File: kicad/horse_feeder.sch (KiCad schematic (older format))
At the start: 50 parts

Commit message: Update schematic
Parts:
- removed RV?: R_POT, symbol Device:R_POT
- removed U?: DS3231MZ, Package_SO:SOIC-8_3.9x4.9mm_P1.27mm, symbol Timer_RTC:DS3231MZ
- removed U?: NHD-0420H1Z, Display:NHD-0420H1Z, symbol Display_Character:NHD-0420H1Z
- added C?: C, symbol Device:C
- added D?: D, symbol Device:D
- added R? (x2): R, symbol Device:R
- added U?: NHD-C0220BIZ, Display:NHD-C0220BiZ, symbol Display_Character:NHD-C0220BIZ
- U? (x3): symbol custom_parts:TC4426ACPA -> horse_feeder-rescue:TC4426ACPA-custom_parts
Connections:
- net labels added: 3.3V, DPD_PIN
- net labels removed: LCD4, LCD5, LCD6, LCD7, LCD_BUS, LCD_EN, LCD_RS, LCD_RW, LOCKBUS
- wire segments 186 -> 166
- no-connect marks 22 -> 20
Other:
- moved on the sheet: R?, SW?

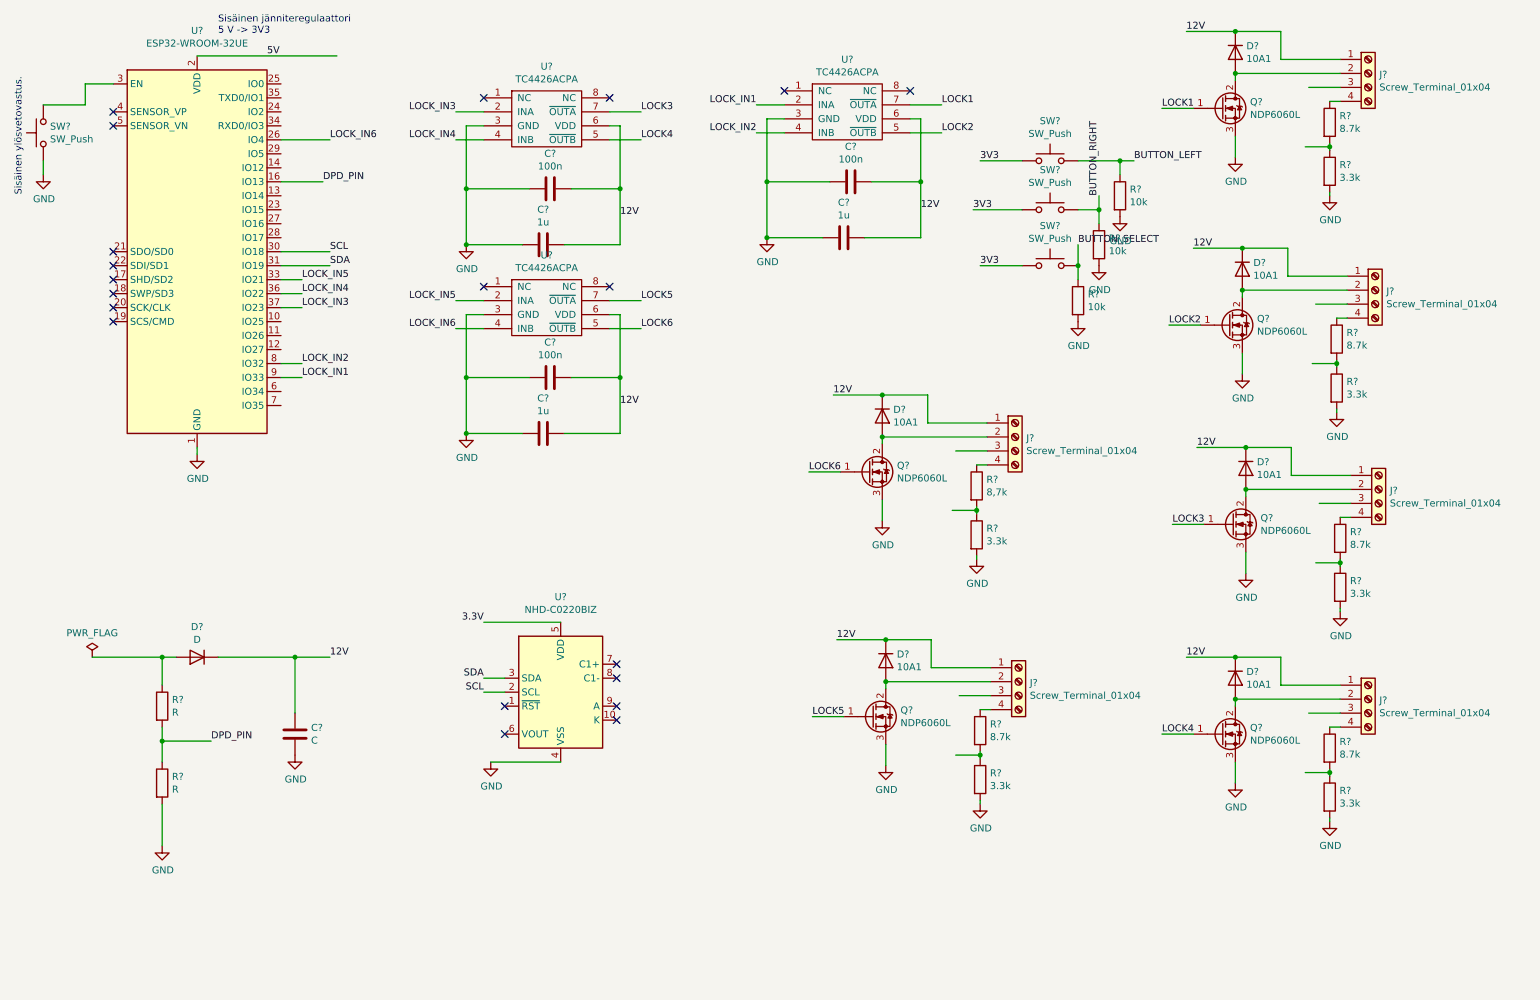
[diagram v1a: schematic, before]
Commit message: Modified schematic and PCB
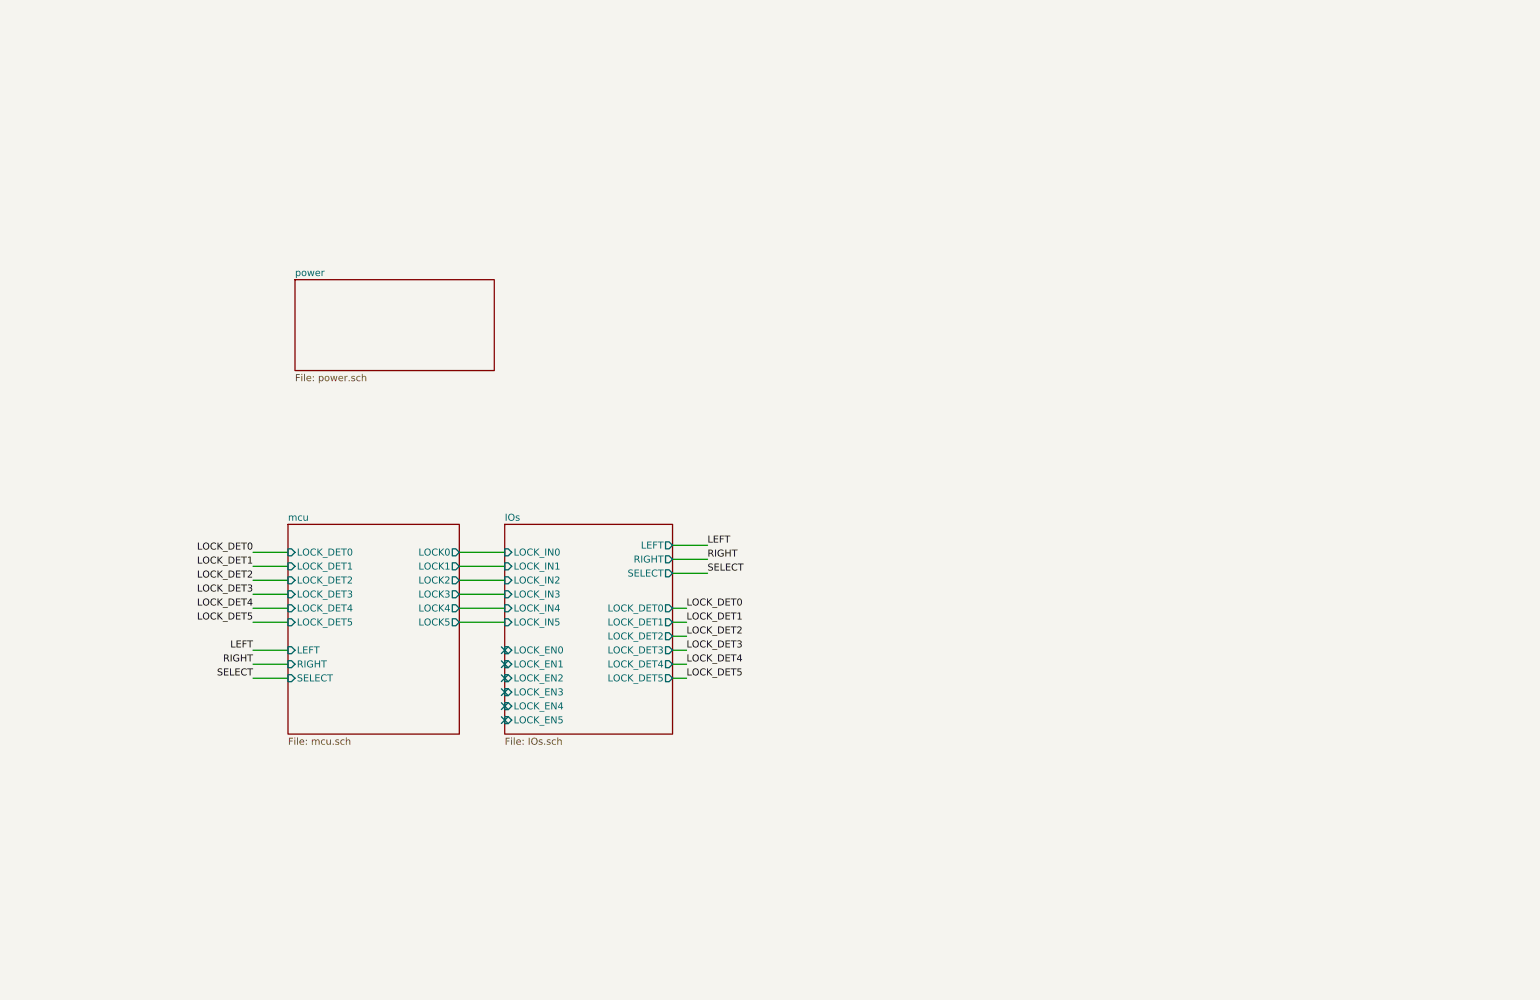
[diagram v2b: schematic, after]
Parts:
- removed C? (x3): 100n, symbol Device:C
- removed C? (x3): 1u, symbol Device:C
- removed C?: C, symbol Device:C
- removed D? (x6): 10A1, symbol Device:D
- removed D?: D, symbol Device:D
- removed J? (x6): Screw_Terminal_01x04, symbol Connector:Screw_Terminal_01x04
- removed Q? (x6): NDP6060L, symbol Device:Q_NMOS_GDS
- removed R? (x5): 8.7k, symbol Device:R
- removed R? (x6): 3.3k, symbol Device:R
- removed R?: 8,7k, symbol Device:R
- removed R? (x2): R, symbol Device:R
- removed R? (x3): 10k, symbol Device:R
- removed SW? (x4): SW_Push, symbol Switch:SW_Push
- removed U? (x3): TC4426ACPA, symbol horse_feeder-rescue:TC4426ACPA-custom_parts
- removed U?: ESP32-WROOM-32UE, RF_Module:ESP32-WROOM-32U, symbol RF_Module:ESP32-WROOM-32U
- removed U?: NHD-C0220BIZ, Display:NHD-C0220BiZ, symbol Display_Character:NHD-C0220BIZ
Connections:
- net labels added: LEFT, LOCK_DET0, LOCK_DET1, LOCK_DET2, LOCK_DET3, LOCK_DET4, LOCK_DET5, RIGHT, SELECT
- net labels removed: 12V, 3.3V, 3V3, 5V, BUTTON_LEFT, BUTTON_RIGHT, BUTTON_SELECT, DPD_PIN, GND, LOCK1, LOCK2, LOCK3, LOCK4, LOCK5, LOCK6, LOCK_IN1, LOCK_IN2, LOCK_IN3, LOCK_IN4, LOCK_IN5, LOCK_IN6, SCL, SDA
- wire segments 166 -> 24
- no-connect marks 20 -> 6
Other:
- note removed: "Sisäinen jänniteregulaattori\n5 V -> 3V3"
- note removed: "Sisäinen ylösvetovastus.\n"
